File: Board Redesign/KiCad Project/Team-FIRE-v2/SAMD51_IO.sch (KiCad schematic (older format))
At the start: 23 parts

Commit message: Fix: connection of IO-RI
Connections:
- net IO-RI: now also U?.66 (PB18)
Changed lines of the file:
@@
 Text GLabel 1260 2390 0    50   Input ~ 0
 IO-DCD
-Text GLabel 3510 3350 0    50   Input ~ 0
+Text GLabel 3980 2630 0    50   Input ~ 0
 IO-RI
 Text GLabel 1260 2590 0    50   Input ~ 0

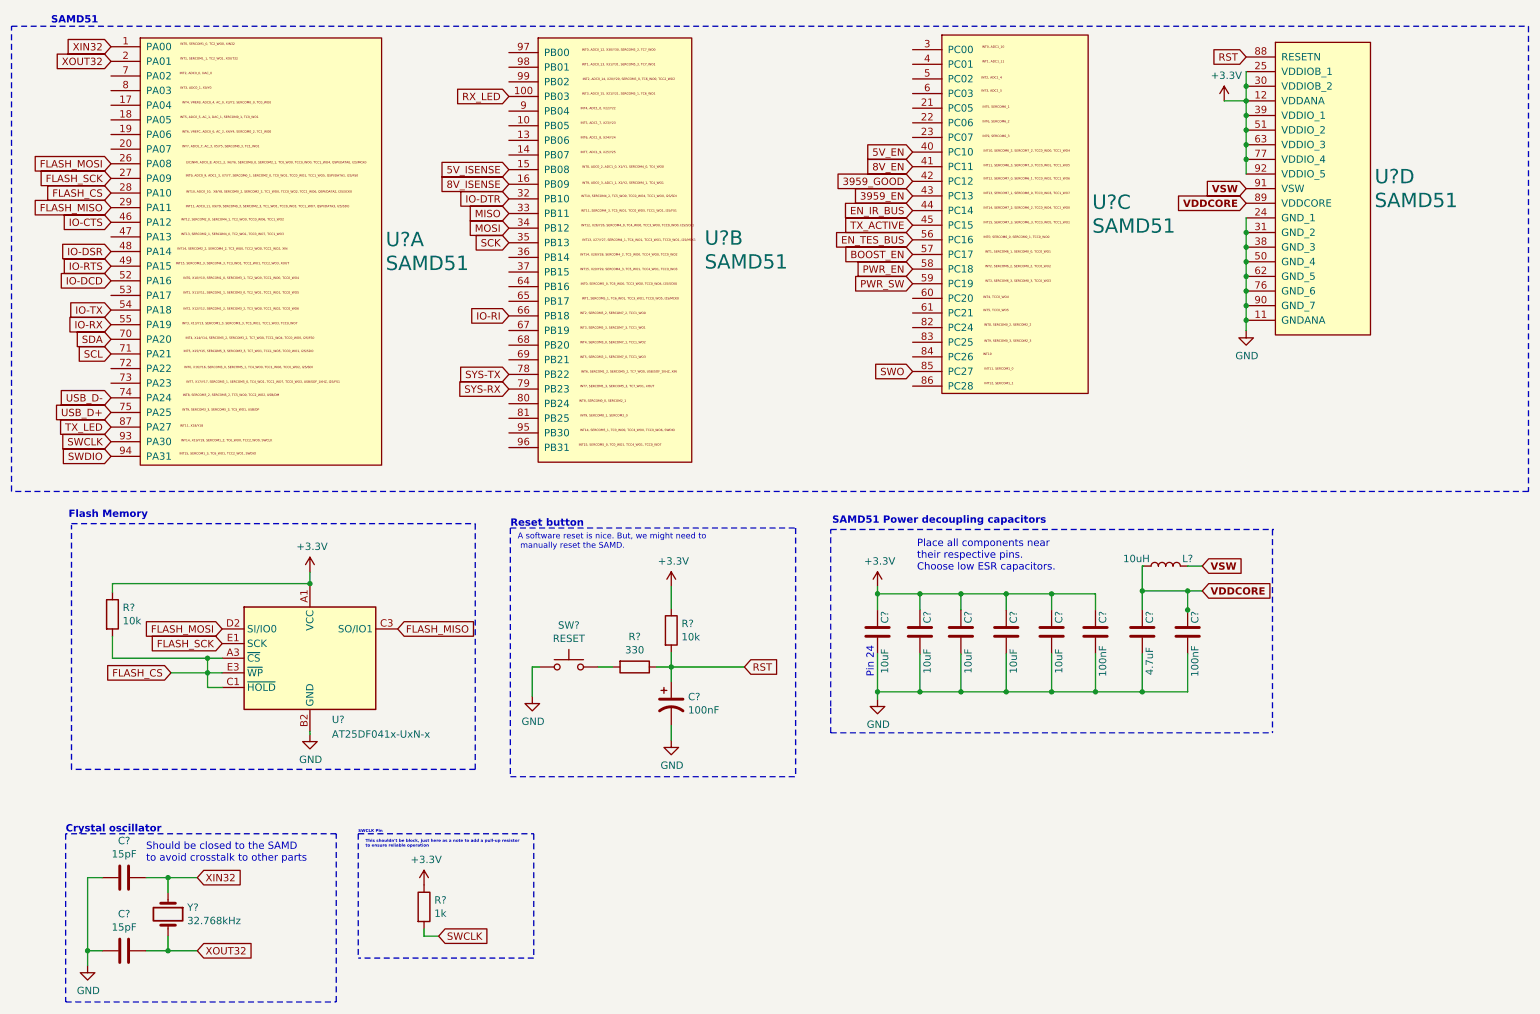
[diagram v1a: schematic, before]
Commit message: Starting complete BOM generation
- Finished schematic(s)
- Started BOM information assignment for final BOM sent to NASA
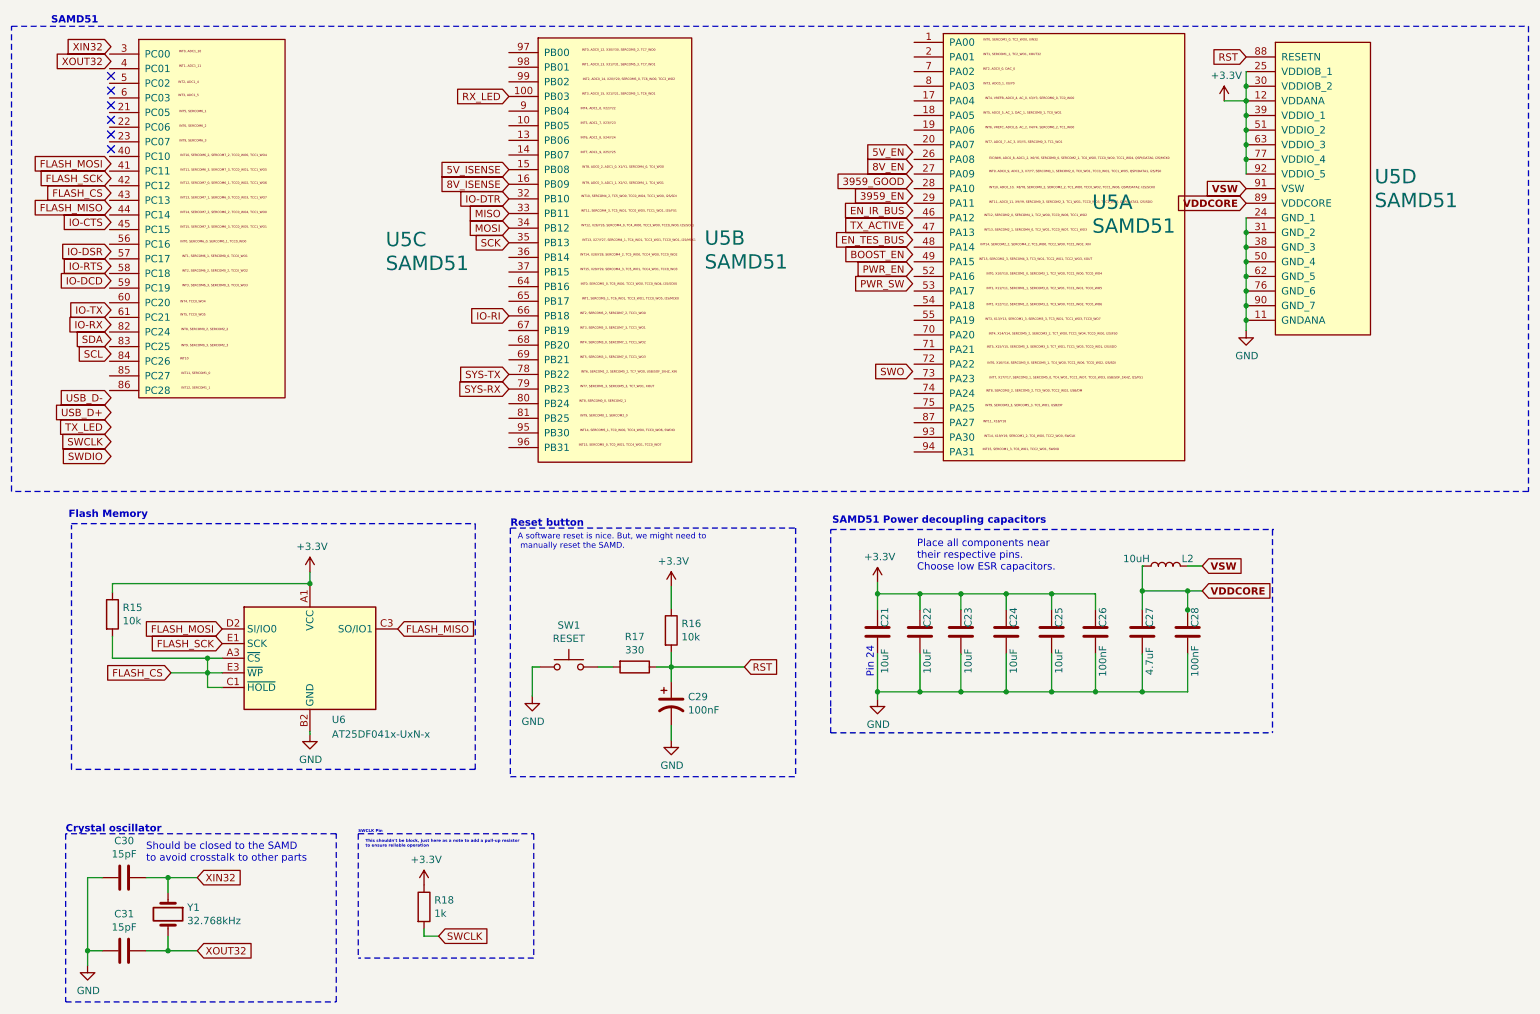
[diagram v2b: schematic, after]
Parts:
- C29: renamed from C?; footprint (none) -> Capacitor_SMD:C_0603_1608Metric
- R16, R17, R18: renamed from R?; footprint (none) -> Resistor_SMD:R_0603_1608Metric
- SW1: renamed from SW?; footprint (none) -> Button_Switch_SMD:SW_SPST_EVQQ2; MPN (none) -> EVQ-Q2Y03W
- gave numbers to parts that had none: 15
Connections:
- net 3959_EN: no longer U5.43 (PC13)
- net 3959_GOOD: no longer U5.42 (PC12)
- net 5V_EN: no longer U5.40 (PC10)
- net 8V_EN: no longer U5.41 (PC11)
- net BOOST_EN: no longer U5.57 (PC17)
- net EN_IR_BUS: no longer U5.44 (PC14)
- net EN_TES_BUS: no longer U5.56 (PC16)
- net FLASH_CS: no longer U5.28 (PA10)
- net FLASH_MISO: no longer U5.29 (PA11)
- net FLASH_MOSI: no longer U5.26 (PA08)
- net FLASH_SCK: no longer U5.27 (PA09)
- net IO-CTS: no longer U5.46 (PA12)
- net IO-DCD: no longer U5.52 (PA16)
- net IO-DSR: no longer U5.48 (PA14)
- net IO-RTS: no longer U5.49 (PA15)
- net IO-RX: no longer U5.55 (PA19)
- net IO-TX: no longer U5.54 (PA18)
- net PWR_EN: no longer U5.58 (PC18)
- net PWR_SW: no longer U5.59 (PC19)
- net SCL: no longer U5.71 (PA21)
- net SDA: no longer U5.70 (PA20)
- net SWCLK: no longer U5.93 (PA30)
- net SWDIO: no longer U5.94 (PA31)
- net SWO: no longer U5.85 (PC27)
- net TX_ACTIVE: no longer U5.45 (PC15)
- net TX_LED: no longer U5.87 (PA27)
- net USB_D+: no longer U5.75 (PA25)
- net USB_D-: no longer U5.74 (PA24)
- net XIN32: no longer U5.1 (PA00)
- net XOUT32: no longer U5.2 (PA01)
- no-connect marks 0 -> 6

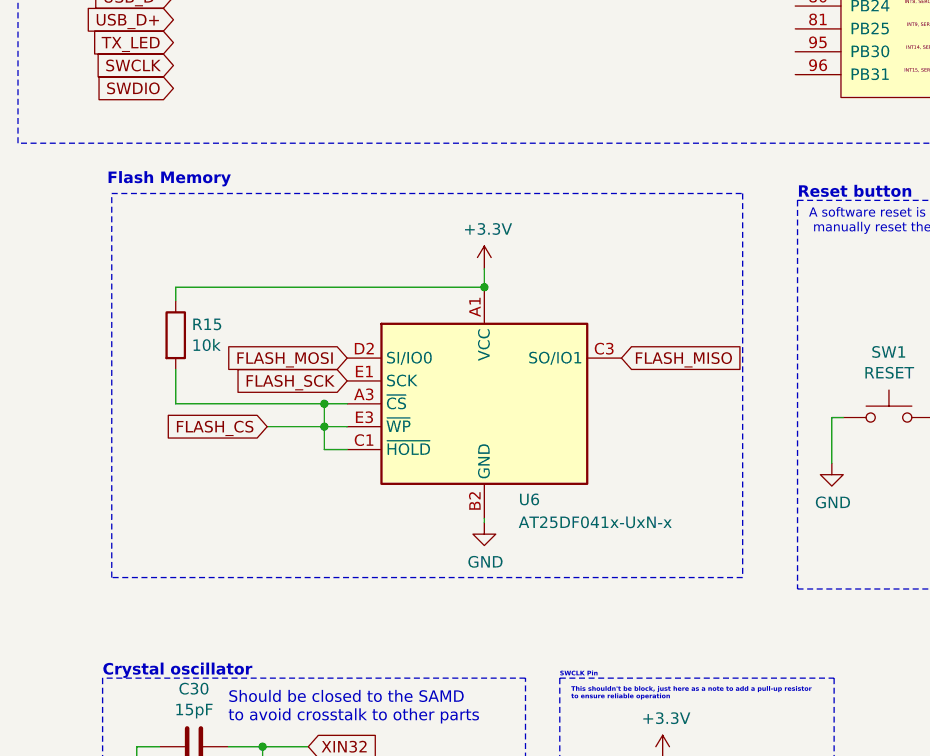
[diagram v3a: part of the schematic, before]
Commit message: Made a lot of changes...
- Added symbol, footprint for Micro USB B connector
- Fixed Flash Memory schematic
- Added details for many components
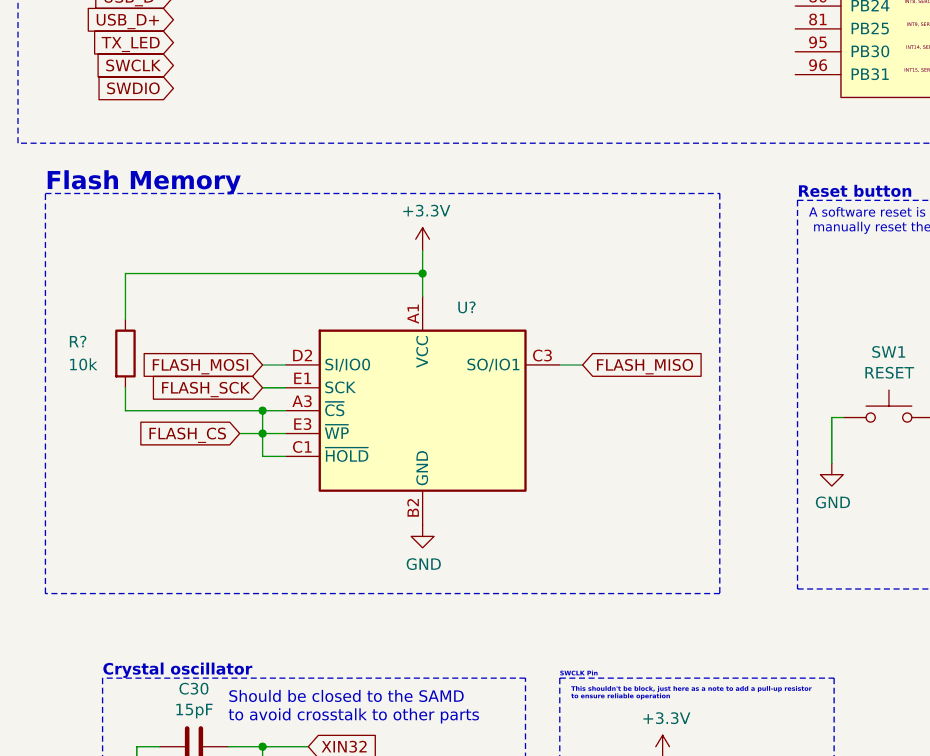
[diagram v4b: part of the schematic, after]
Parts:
- removed R15: 10k, symbol Device:R
- removed U6: AT25DF041x-UxN-x, Package_CSP:WLCSP-8_1.58x1.63x0.35mm_Layout3x5_P0.35x0.4mm_Ball0.25mm_Pad0.25mm_NSMD, symbol Memory_Flash:AT25DF041x-UxN-x
- added R?: 10k, Resistor_SMD:R_0603_1608Metric, symbol Device:R
- added U?: AT25DF041x-UxN-x, Package_CSP:WLCSP-8_1.58x1.63x0.35mm_Layout3x5_P0.35x0.4mm_Ball0.25mm_Pad0.25mm_NSMD, symbol Memory_Flash:AT25DF041x-UxN-x
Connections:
- net +3V3: now also R?.1, U?.A1 (VCC)
- net FLASH_CS: now also R?.2, U?.A3 (~CS), U?.C1 (~HOLD~), U?.E3 (~WP~)
- net FLASH_MISO: now also U?.C3 (SO/IO1)
- net FLASH_MOSI: now also U?.D2 (SI/IO0)
- net FLASH_SCK: now also U?.E1 (SCK)
- net GND: now also U?.B2 (GND)
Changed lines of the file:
@@
 Text Notes 6190 4060 0    50   ~ 10
 SAMD51 Power decoupling capacitors
-$Comp
-L Memory_Flash:AT25DF041x-UxN-x U?
-U 1 1 5F15C396
-P 2620 4970
-AR Path="/5E4F8378/5EA71818/5F15C396" Ref="U?"  Part="1"
-AR Path="/5E4F8378/5ED4DEFC/5ED7D75E/5F15C396" Ref="U?"  Part="1"
-AR Path="/5E4F8378/5ED4DEFC/5F15C396" Ref="U6"  Part="1"
-F 0 "U6" H 2770 4550 50  0000 L CNN
-F 1 "AT25DF041x-UxN-x" H 2770 4450 50  0000 L CNN
-F 2 "Package_CSP:WLCSP-8_1.58x1.63x0.35mm_Layout3x5_P0.35x0.4mm_Ball0.25mm_Pad0.25mm_NSMD" H 2420 4370 50  0001 C CNN
-F 3 "http://www.adestotech.com/wp-content/uploads/DS-AT25DF041B_040.pdf" H 2620 5670 50  0001 C CNN
-	1    2620 4970
-	1    0    0    -1
-$EndComp
-Text GLabel 3220 4770 2    50   Input ~ 0
+Text GLabel 3050 4800 2    50   Input ~ 0
 FLASH_MISO
-Text GLabel 2020 4870 0    50   Input ~ 0
-FLASH_SCK
-Text GLabel 2020 4770 0    50   Input ~ 0
-FLASH_MOSI
-Wire Wire Line
-	2620 5490 2620 5470
 $Comp
 L power:+3.3V #PWR?
 U 1 1 5F15C3A7
-P 2620 4380
+P 2350 4300
 AR Path="/5E4F8378/5EA71818/5F15C3A7" Ref="#PWR?"  Part="1"
 AR Path="/5E4F8378/5ED4DEFC/5ED7D75E/5F15C3A7" Ref="#PWR?"  Part="1"
 AR Path="/5E4F8378/5ED4DEFC/5F15C3A7" Ref="#PWR0138"  Part="1"
-F 0 "#PWR0138" H 2620 4230 50  0001 C CNN
-F 1 "+3.3V" H 2635 4553 50  0000 C CNN
-F 2 "" H 2620 4380 50  0001 C CNN
-F 3 "" H 2620 4380 50  0001 C CNN
-	1    2620 4380
-	1    0    0    -1
-$EndComp
-Wire Wire Line
-	2620 4380 2620 4460
-Wire Wire Line
-	2020 4970 1920 4970
-Wire Wire Line
-	2020 5070 1920 5070
-Wire Wire Line
-	1920 5070 1920 4970
-Connection ~ 1920 4970
-Wire Wire Line
-	1920 5070 1670 5070
-Connection ~ 1920 5070
-Connection ~ 2620 4460
-Wire Wire Line
-	2620 4460 2620 4470
-Wire Wire Line
-	1270 4820 1270 4970
-Wire Wire Line
-	1270 4520 1270 4460
-Wire Wire Line
-	2020 5170 1920 5170
-Wire Wire Line
-	1920 5170 1920 5070
-Wire Wire Line
-	1270 4460 2620 4460
-Wire Wire Line
-	1270 4970 1920 4970
-Text Notes 970  4020 0    50   ~ 10
-Flash Memory
+F 0 "#PWR0138" H 2350 4150 50  0001 C CNN
+F 1 "+3.3V" H 2365 4473 50  0000 C CNN
+F 2 "" H 2350 4300 50  0001 C CNN
+F 3 "" H 2350 4300 50  0001 C CNN
+	1    2350 4300
+	1    0    0    -1
+$EndComp
 $Comp
 L Device:Crystal Y?
@@
 Wire Notes Line
 	3990 4080 5940 4080
-Wire Notes Line
-	990  4050 3750 4050
-Wire Notes Line
-	3750 4050 3750 5730
-Wire Notes Line
-	3750 5730 990  5730
-Wire Notes Line
-	990  5730 990  4060
 Connection ~ 8620 4640
 Wire Wire Line
@@
 	1    0    0    -1
 $EndComp
-$Comp
-L Device:R R?
-U 1 1 5F15C3AE
-P 1270 4670
-AR Path="/5E4F8378/5EA71818/5F15C3AE" Ref="R?"  Part="1"
-AR Path="/5E4F8378/5ED4DEFC/5ED7D75E/5F15C3AE" Ref="R?"  Part="1"
-AR Path="/5E4F8378/5ED4DEFC/5F15C3AE" Ref="R15"  Part="1"
-F 0 "R15" H 1340 4716 50  0000 L CNN
-F 1 "10k" H 1340 4625 50  0000 L CNN
-F 2 "" V 1200 4670 50  0001 C CNN
-F 3 "~" H 1270 4670 50  0001 C CNN
-	1    1270 4670
-	1    0    0    -1
-$EndComp
 NoConn ~ 1260 990
 NoConn ~ 1260 1090
@@
 NoConn ~ 1260 1390
 NoConn ~ 1260 1490
-Text GLabel 1670 5070 0    50   Input ~ 0
-FLASH_CS
 Text GLabel 1850 6470 2    50   Input ~ 0
 XIN32
 $Comp
+L Memory_Flash:AT25DF041x-UxN-x U?
+U 1 1 5EBC3761
+P 2350 5000
+F 0 "U?" H 2500 5450 50  0000 L CNN
+F 1 "AT25DF041x-UxN-x" H 2994 4955 50  0001 L CNN
+F 2 "Package_CSP:WLCSP-8_1.58x1.63x0.35mm_Layout3x5_P0.35x0.4mm_Ball0.25mm_Pad0.25mm_NSMD" H 2150 4400 50  0001 C CNN
+F 3 "http://www.adestotech.com/wp-content/uploads/DS-AT25DF041B_040.pdf" H 2350 5700 50  0001 C CNN
+	1    2350 5000
+	1    0    0    -1
+$EndComp
+Wire Wire Line
+	1750 4800 1650 4800
+Text GLabel 1550 5100 0    50   Input ~ 0
+FLASH_CS
+Wire Wire Line
+	1750 5100 1650 5100
+Wire Wire Line
+	1750 5200 1650 5200
+Wire Wire Line
+	1650 5000 1750 5000
+Wire Wire Line
+	1650 5000 1650 5100
+Connection ~ 1650 5100
+Wire Wire Line
+	1650 5100 1550 5100
+Wire Wire Line
+	1650 5100 1650 5200
+Wire Wire Line
+	2350 4300 2350 4400
+Wire Wire Line
+	2950 4800 3050 4800
+$Comp
 L power:GND #PWR?
-U 1 1 5F15C3A0
-P 2620 5490
-AR Path="/5E4F8378/5EA71818/5F15C3A0" Ref="#PWR?"  Part="1"
-AR Path="/5E4F8378/5ED4DEFC/5ED7D75E/5F15C3A0" Ref="#PWR?"  Part="1"
-AR Path="/5E4F8378/5ED4DEFC/5F15C3A0" Ref="#PWR0137"  Part="1"
-F 0 "#PWR0137" H 2620 5240 50  0001 C CNN
-F 1 "GND" H 2625 5317 50  0000 C CNN
-F 2 "" H 2620 5490 50  0001 C CNN
-F 3 "" H 2620 5490 50  0001 C CNN
-	1    2620 5490
-	1    0    0    -1
-$EndComp
+U 1 1 5EBDC8BA
+P 2350 5500
+AR Path="/5E4F8378/5EA71818/5EBDC8BA" Ref="#PWR?"  Part="1"
+AR Path="/5E4F8378/5ED4DEFC/5ED7D75E/5EBDC8BA" Ref="#PWR?"  Part="1"
+AR Path="/5E4F8378/5ED4DEFC/5EBDC8BA" Ref="#PWR?"  Part="1"
+F 0 "#PWR?" H 2350 5250 50  0001 C CNN
+F 1 "GND" H 2355 5327 50  0000 C CNN
+F 2 "" H 2350 5500 50  0001 C CNN
+F 3 "" H 2350 5500 50  0001 C CNN
+	1    2350 5500
+	1    0    0    -1
+$EndComp
+Wire Wire Line
+	1650 4900 1750 4900
+Text GLabel 1650 4900 0    50   Input ~ 0
+FLASH_SCK
+Text GLabel 1650 4800 0    50   Input ~ 0
+FLASH_MOSI
+$Comp
+L Device:R R?
+U 1 1 5EBDEFB3
+P 1050 4750
+AR Path="/5E4F8378/5EBDEFB3" Ref="R?"  Part="1"
+AR Path="/5E4F8378/5ED4DEFC/5EBDEFB3" Ref="R?"  Part="1"
+F 0 "R?" H 800 4800 50  0000 L CNN
+F 1 "10k" H 800 4700 50  0000 L CNN
+F 2 "Resistor_SMD:R_0603_1608Metric" V 980 4750 50  0001 C CNN
+F 3 "https://www.mouser.com/datasheet/2/427/mcx0x0xpre-1762843.pdf" H 1050 4750 50  0001 C CNN
+F 4 "MCT06030E1002BP100" H 1050 4750 50  0001 C CNN "MPN"
+F 5 "Vishay" H 1050 4750 50  0001 C CNN "Manufacturer"
+F 6 "Mouser" H 1050 4750 50  0001 C CNN "Supplier"
+F 7 "594-MCT06030E1002BP1" H 1050 4750 50  0001 C CNN "Supplier PN"
+F 8 "https://www.mouser.com/ProductDetail/Vishay-Beyschlag/MCT06030E1002BP100?qs=sGAEpiMZZMtlubZbdhIBIHIEm3drdiPa32EPxwxqfD0%3D" H 1050 4750 50  0001 C CNN "Link"
+F 9 "Thin Film Resistor" H 1050 4750 50  0001 C CNN "Type"
+F 10 "0.1%" H 1050 4750 50  0001 C CNN "Tolerance"
+F 11 "75 V" H 1050 4750 50  0001 C CNN "Voltage Rating"
+	1    1050 4750
+	1    0    0    -1
+$EndComp
+Wire Wire Line
+	1650 5000 1050 5000
+Wire Wire Line
+	1050 5000 1050 4900
+Connection ~ 1650 5000
+Wire Wire Line
+	1050 4600 1050 4400
+Wire Wire Line
+	1050 4400 2350 4400
+Connection ~ 2350 4400
+Wire Wire Line
+	2350 4400 2350 4500
+Wire Notes Line
+	700  4050 3650 4050
+Wire Notes Line
+	3650 4050 3650 5800
+Wire Notes Line
+	3650 5800 700  5800
+Wire Notes Line
+	700  5800 700  4050
+Text Notes 700  4050 0    79   ~ 16
+Flash Memory
 $EndSCHEMATC

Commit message: fixed issue
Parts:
- gave numbers to parts that had none: 2
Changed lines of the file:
@@
 Comment4 ""
 $EndDescr
-Text GLabel 1260 3190 0    50   Input ~ 0
-USB_D-
-Text GLabel 1260 3290 0    50   Input ~ 0
-USB_D+
-Text GLabel 1260 2790 0    50   Input ~ 0
-SDA
-Text GLabel 1260 2890 0    50   Input ~ 0
-SCL
 $Comp
 L Team-FIRE:SAMD51 U?
@@
 	1    0    0    -1
 $EndComp
-Text GLabel 1260 3490 0    50   Input ~ 0
-SWCLK
-Text GLabel 1260 3590 0    50   Input ~ 0
-SWDIO
 Text GLabel 3980 1130 0    50   Input ~ 0
 RX_LED
-Text GLabel 1260 3390 0    50   Input ~ 0
-TX_LED
 Text GLabel 6740 3010 0    50   Input ~ 0
 SWO
@@
 	8310 4510 8310 4640
 Connection ~ 8620 4510
-Text GLabel 1260 1590 0    50   Input ~ 0
-FLASH_MOSI
-Text GLabel 1260 1790 0    50   Input ~ 0
-FLASH_CS
-Text GLabel 1260 1890 0    50   Input ~ 0
-FLASH_MISO
-Text GLabel 1260 1690 0    50   Input ~ 0
-FLASH_SCK
-Text GLabel 1260 2290 0    50   Input ~ 0
-IO-RTS
-Text GLabel 1260 1990 0    50   Input ~ 0
-IO-CTS
-Text GLabel 1260 2190 0    50   Input ~ 0
-IO-DSR
-Text GLabel 1260 2390 0    50   Input ~ 0
-IO-DCD
 Text GLabel 3980 2630 0    50   Input ~ 0
 IO-RI
-Text GLabel 1260 2590 0    50   Input ~ 0
-IO-TX
-Text GLabel 1260 2690 0    50   Input ~ 0
-IO-RX
 Text GLabel 3980 1830 0    50   Input ~ 0
 IO-DTR
@@
 Text GLabel 1850 6470 2    50   Input ~ 0
 XIN32
-$Comp
-L Memory_Flash:AT25DF041x-UxN-x U?
-U 1 1 5EBC3761
-P 2350 5000
-F 0 "U?" H 2500 5450 50  0000 L CNN
-F 1 "AT25DF041x-UxN-x" H 2994 4955 50  0001 L CNN
-F 2 "Package_CSP:WLCSP-8_1.58x1.63x0.35mm_Layout3x5_P0.35x0.4mm_Ball0.25mm_Pad0.25mm_NSMD" H 2150 4400 50  0001 C CNN
-F 3 "http://www.adestotech.com/wp-content/uploads/DS-AT25DF041B_040.pdf" H 2350 5700 50  0001 C CNN
-	1    2350 5000
-	1    0    0    -1
-$EndComp
 Wire Wire Line
 	1750 4800 1650 4800
@@
 AR Path="/5E4F8378/5EA71818/5EBDC8BA" Ref="#PWR?"  Part="1"
 AR Path="/5E4F8378/5ED4DEFC/5ED7D75E/5EBDC8BA" Ref="#PWR?"  Part="1"
-AR Path="/5E4F8378/5ED4DEFC/5EBDC8BA" Ref="#PWR?"  Part="1"
-F 0 "#PWR?" H 2350 5250 50  0001 C CNN
+AR Path="/5E4F8378/5ED4DEFC/5EBDC8BA" Ref="#PWR013"  Part="1"
+F 0 "#PWR013" H 2350 5250 50  0001 C CNN
 F 1 "GND" H 2355 5327 50  0000 C CNN
 F 2 "" H 2350 5500 50  0001 C CNN
@@
 P 1050 4750
 AR Path="/5E4F8378/5EBDEFB3" Ref="R?"  Part="1"
-AR Path="/5E4F8378/5ED4DEFC/5EBDEFB3" Ref="R?"  Part="1"
-F 0 "R?" H 800 4800 50  0000 L CNN
+AR Path="/5E4F8378/5ED4DEFC/5EBDEFB3" Ref="R15"  Part="1"
+F 0 "R15" H 800 4800 50  0000 L CNN
 F 1 "10k" H 800 4700 50  0000 L CNN
 F 2 "Resistor_SMD:R_0603_1608Metric" V 980 4750 50  0001 C CNN
@@
 Text Notes 700  4050 0    79   ~ 16
 Flash Memory
+$Comp
+L Memory_Flash:AT25DF041x-UxN-x U6
+U 1 1 5EBC3761
+P 2350 5000
+F 0 "U6" H 2500 5450 50  0000 L CNN
+F 1 "AT25DF041x-UxN-x" H 2994 4955 50  0001 L CNN
+F 2 "Package_CSP:WLCSP-8_1.58x1.63x0.35mm_Layout3x5_P0.35x0.4mm_Ball0.25mm_Pad0.25mm_NSMD" H 2150 4400 50  0001 C CNN
+F 3 "http://www.adestotech.com/wp-content/uploads/DS-AT25DF041B_040.pdf" H 2350 5700 50  0001 C CNN
+	1    2350 5000
+	1    0    0    -1
+$EndComp
+Text GLabel 1260 2740 0    50   Input ~ 0
+USB_D-
+Text GLabel 1260 2840 0    50   Input ~ 0
+USB_D+
+Text GLabel 1260 2340 0    50   Input ~ 0
+SDA
+Text GLabel 1260 2440 0    50   Input ~ 0
+SCL
+Text GLabel 1260 3040 0    50   Input ~ 0
+SWCLK
+Text GLabel 1260 3140 0    50   Input ~ 0
+SWDIO
+Text GLabel 1260 2940 0    50   Input ~ 0
+TX_LED
+Text GLabel 1260 1140 0    50   Input ~ 0
+FLASH_MOSI
+Text GLabel 1260 1340 0    50   Input ~ 0
+FLASH_CS
+Text GLabel 1260 1440 0    50   Input ~ 0
+FLASH_MISO
+Text GLabel 1260 1240 0    50   Input ~ 0
+FLASH_SCK
+Text GLabel 1260 1840 0    50   Input ~ 0
+IO-RTS
+Text GLabel 1260 1540 0    50   Input ~ 0
+IO-CTS
+Text GLabel 1260 1740 0    50   Input ~ 0
+IO-DSR
+Text GLabel 1260 1940 0    50   Input ~ 0
+IO-DCD
+Text GLabel 1260 2140 0    50   Input ~ 0
+IO-TX
+Text GLabel 1260 2240 0    50   Input ~ 0
+IO-RX
 $EndSCHEMATC
